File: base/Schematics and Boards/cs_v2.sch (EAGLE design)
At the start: 80 parts, among them J101 J-JTAG-CORTEX-NEEDLE6, J301 HIROSE-DF40_44-PIN_CONNECTORS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, J302 HIROSE-DF40_30-PIN_CONNECTORS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, Q201 FK3303010L, Q202 FK3303010L, Q203 FK3303010L, Q204 DMG3415UFY4Q-7, U1 AT25SF641-MHB-T, U101 ATSAMD51, U201 COULOMB-MAX17262, U202 CUS520H3F, U203 MAX77827BEWC+T, U204 SENSOR-SI7006, U205 LOADSWITCH-MIC94164, U206 LOADSWITCH-MIC94164, Y101 16M, Y102 ABS07-32.768KHZ-9-T

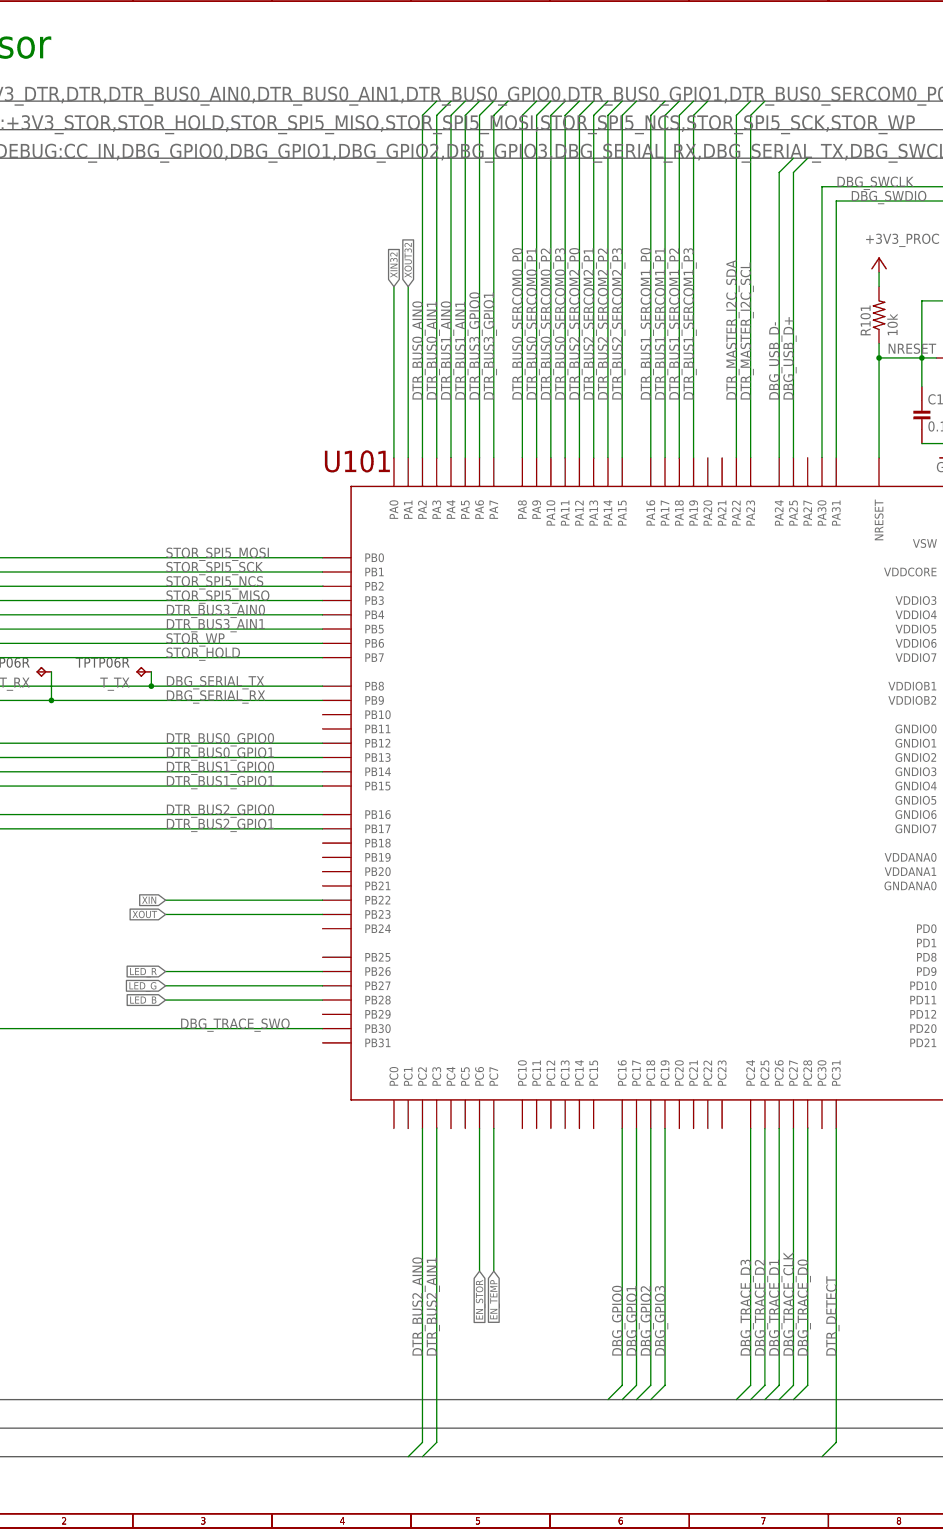
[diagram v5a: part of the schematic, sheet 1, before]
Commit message: Manual route power traces, lock traces/vias before autoroute
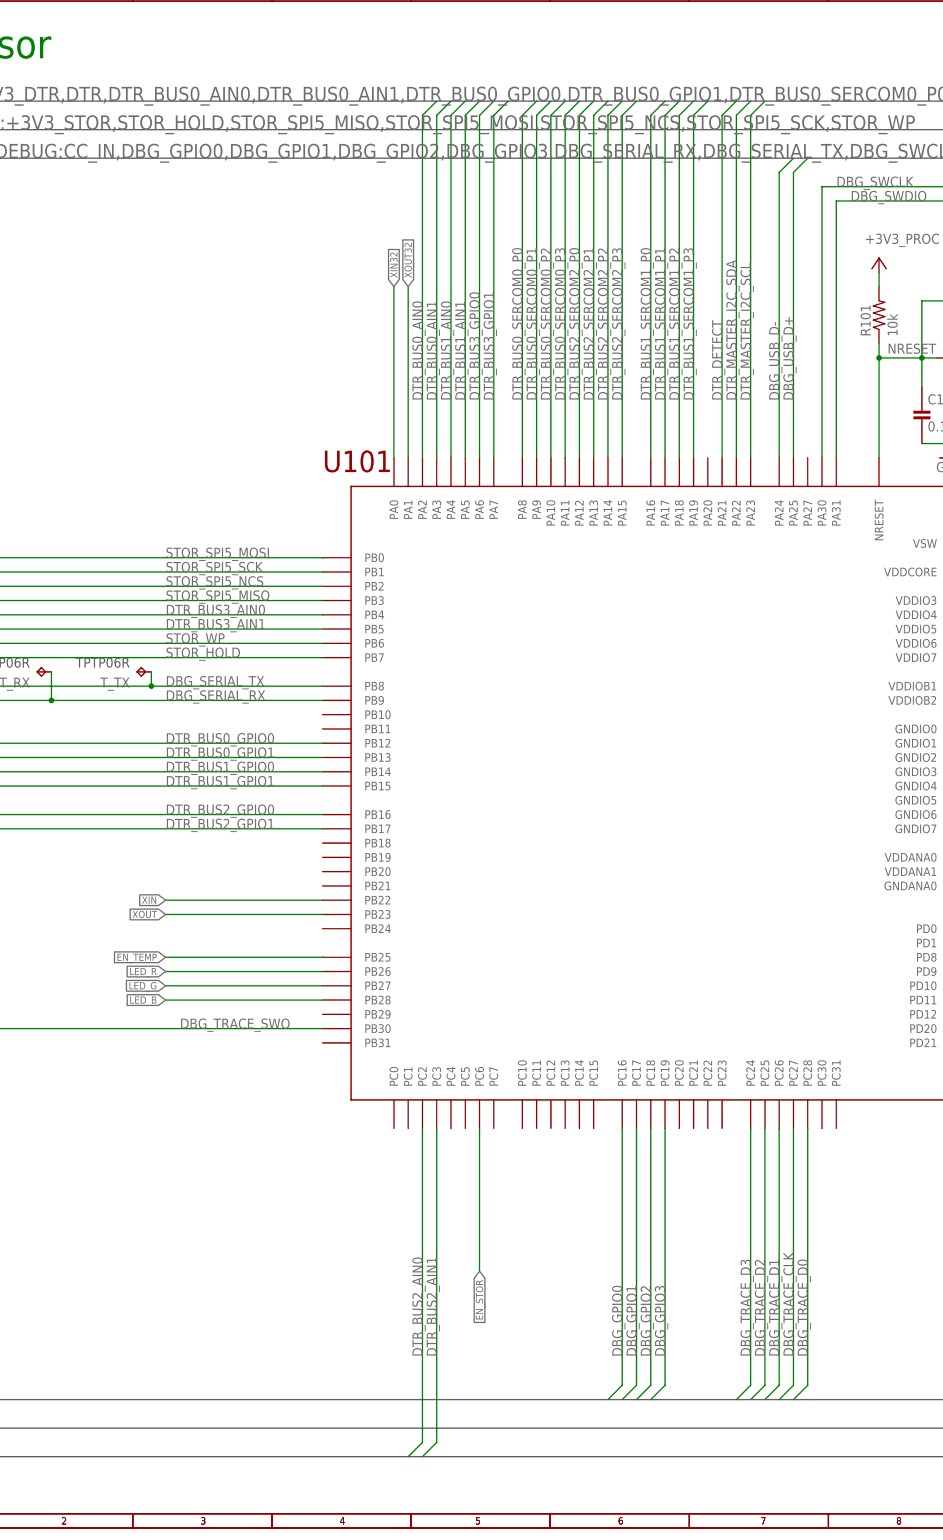
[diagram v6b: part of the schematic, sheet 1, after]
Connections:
- net DTR_DETECT: now also U101.PA21; no longer U101.PC31
- net EN_TEMP: now also U101.PB25; no longer U101.PC7
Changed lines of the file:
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@@
 <net name="DTR_DETECT" class="0">
 <segment>
-<pinref part="U101" gate="G$1" pin="PC31"/>
-<wire x1="175.26" y1="71.12" x2="175.26" y2="15.24" width="0.1524" layer="91"/>
-<label x="175.26" y="30.48" size="1.778" layer="95" rot="R90"/>
-<wire x1="175.26" y1="15.24" x2="172.72" y2="12.7" width="0.1524" layer="91"/>
+<pinref part="U101" gate="G$1" pin="PA21"/>
+<label x="154.94" y="200.66" size="1.778" layer="95" rot="R90"/>
+<wire x1="154.94" y1="190.5" x2="154.94" y2="251.46" width="0.1524" layer="91"/>
+<wire x1="154.94" y1="251.46" x2="157.48" y2="254" width="0.1524" layer="91"/>
 </segment>
 </net>
@@
 <net name="EN_TEMP" class="0">
 <segment>
-<pinref part="U101" gate="G$1" pin="PC7"/>
-<wire x1="114.3" y1="71.12" x2="114.3" y2="45.72" width="0.1524" layer="91"/>
-<label x="114.3" y="45.72" size="1.27" layer="95" rot="R270" xref="yes"/>
+<pinref part="U101" gate="G$1" pin="PB25"/>
+<wire x1="83.82" y1="101.6" x2="55.88" y2="101.6" width="0.1524" layer="91"/>
+<label x="55.88" y="101.6" size="1.27" layer="95" rot="R180" xref="yes"/>
 </segment>
 </net>

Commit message: Renumber parts and remove unneeded silk
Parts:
- removed JP_PROC: JUMPER-SMT_2_NC_PASTE_NO-SILK, Connectors:JUMPER-SMT_2_NC_PASTE_NO-SILK
- removed R112: 1k, Resistors:R-0402
- removed U206: LOADSWITCH-MIC94164, Switches:LOADSWITCH-MIC94164
- added D202: DIALIGHT_RGBLED_598-8710-307FDIALIGHT_598-8710-307F_0_0, Diodes:DIALIGHT_RGBLED_598-8710-307FDIALIGHT_598-8710-307F_0_0
- added JP205: JUMPER-SMT_2_NC_PASTE_NO-SILK, Connectors:JUMPER-SMT_2_NC_PASTE_NO-SILK
- added R105: 39, Resistors:R-0402
- D201: value DIALIGHT_RGBLED_598-8710-307FDIALIGHT_598-8710-307F_0_0 -> CUS520H3F; device Diodes:DIALIGHT_RGBLED_598-8710-307FDIALIGHT_598-8710-307F_0_0 -> Diodes:CUS520H3F; PART_NO 598-8710-307F -> (none)
- Q202: value FK3303010L -> DMG3415UFY4Q-7; device Switches:FK3303010L -> Switches:DMG3415UFY4Q-7; PART_NO (none) -> DMG3415UFY4Q-7
- Q204: value DMG3415UFY4Q-7 -> FK3303010L; device Switches:DMG3415UFY4Q-7 -> Switches:FK3303010L; PART_NO DMG3415UFY4Q-7 -> (none)
- R106: value 39 -> 1k; PART_NO ERJ-2GEJ390X -> ERJ-2GEJ102X
- R201: value 590 -> 10M; PART_NO ERJ-2RKF5900X -> ERJ-2GEJ106X; TOL 1% -> (none)
- R203: value 1k -> 590; PART_NO ERA-2AED102X -> ERJ-2RKF5900X; TOL 0.5% -> 1%
- R204: value 10M -> 1k; PART_NO ERJ-2GEJ106X -> ERA-2AED102X; TOL (none) -> 0.5%
- U202: value CUS520H3F -> MAX77827BEWC+T; device Diodes:CUS520H3F -> Regulators:MAX77827BEWC+T
- U203: value MAX77827BEWC+T -> SENSOR-SI7006; device Regulators:MAX77827BEWC+T -> Sensors:SENSOR-SI7006
- U204: value SENSOR-SI7006 -> LOADSWITCH-MIC94164; device Sensors:SENSOR-SI7006 -> Switches:LOADSWITCH-MIC94164; MP (none) -> MIC94162YCS-TR; PART_NO (none) -> MIC94162YCS-TR; SPICEPREFIX (none) -> E
- U205: SPICEPREFIX E -> (none)
- renumbered JP1 to JP203, JP_VDBG to JP201, T_COR to TP_CPU, T_CPU to TP_PROC, T_DTR to TP_DTR, T_RX to TP_RX, T_SCL to TP_SCL, T_SDA to TP_SDA, T_STR to TP_STOR, T_TMP to TP_TEMP, T_TX to TP_TX, U1 to U102
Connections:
- removed net N$16 (its old number): Q202.D, R202.2
- new net N$17: Q204.D, R204.2
- net +3V3: now also U202.OUT, U202.OUTS; no longer U203.OUT, U203.OUTS
- net +3V3_DTR: now also JP205.1; no longer JP204.1
- net +3V3_DTR_SENSE: now also JP205.2; no longer JP204.2
- net +3V3_PROC: now also JP204.1, R106.2; no longer JP_PROC.1, R112.2
- net +3V3_PROC_SENSE: now also JP204.2; no longer JP_PROC.2
- net +3V3_STOR: now also U204.VOUT; no longer U205.VOUT
- net +3V3_STOR_SENSE: now also U204.VIN; no longer U205.VIN
- net +3V3_TEMP: now also U203.V, U205.VOUT; no longer U204.V, U206.VOUT
- net +3V3_TEMP_SENSE: now also U205.VIN; no longer U206.VIN
- net +3V7_BATT: now also Q202.D; no longer Q204.D
- net DBG_SWCLK: now also R106.1; no longer R112.1
- net DTR_MASTER_I2C_SCL: now also U203.SCL; no longer U204.SCL
- net DTR_MASTER_I2C_SDA: now also U203.SDA; no longer U204.SDA
- net EN_STOR: now also U204.ENABLE; no longer U205.ENABLE
- net EN_TEMP: now also U205.ENABLE; no longer U206.ENABLE
- net GND: now also Q204.S, R201.1, U202.AGND, U202.FPWM, U202.PGND, U203.GND; no longer Q202.S, R204.1, U203.AGND, U203.FPWM, U203.PGND, U206.GND
- net JTAG_NRESET: now also R105.2; no longer R106.2
- net LED_G: now also Q203.G; no longer Q202.G
- net LED_R: now also Q204.G; no longer Q203.G
- net LED_VIN: now also D202.COMMON_ANODE; no longer D201.COMMON_ANODE
- net N$12: now also D202.GREEN_CATHODE, R203.1; no longer D201.GREEN_CATHODE, R202.1
- net N$14: now also D202.RED_CATHODE, R204.1; no longer D201.RED_CATHODE, R203.1
- net N$15: now also R202.2; no longer R201.2
- net N$4: now also D202.BLUE_CATHODE, R202.1; no longer D201.BLUE_CATHODE, R201.1
- net NRESET: now also R105.1; no longer R106.1
- net VDD_DBG_JMP: now also D201.P, Q202.G, R201.2; no longer Q204.G, R204.2, U202.P
- net VDD_SW: now also D201.N, Q202.S; no longer Q204.S, U202.N
- net VREG_BIAS: now also U202.BIAS; no longer U203.BIAS
- net VREG_IN: now also U202.EN, U202.IN; no longer U203.EN, U203.IN
- net VREG_LX1: now also U202.LX1; no longer U203.LX1
- net VREG_LX2: now also U202.LX2; no longer U203.LX2
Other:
- moved on the sheet: JP204, Q203, R106, R201, R202, R203, R204, U205
